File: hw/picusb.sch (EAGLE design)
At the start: 38 parts, among them Q1 BSS138, Q2 BSS138, Q3 BSS84, Q4 BSS84, U1 PIC16F1454SOIC, U2 AP7115W, X1 MINI-USB-UX60-MB-5ST

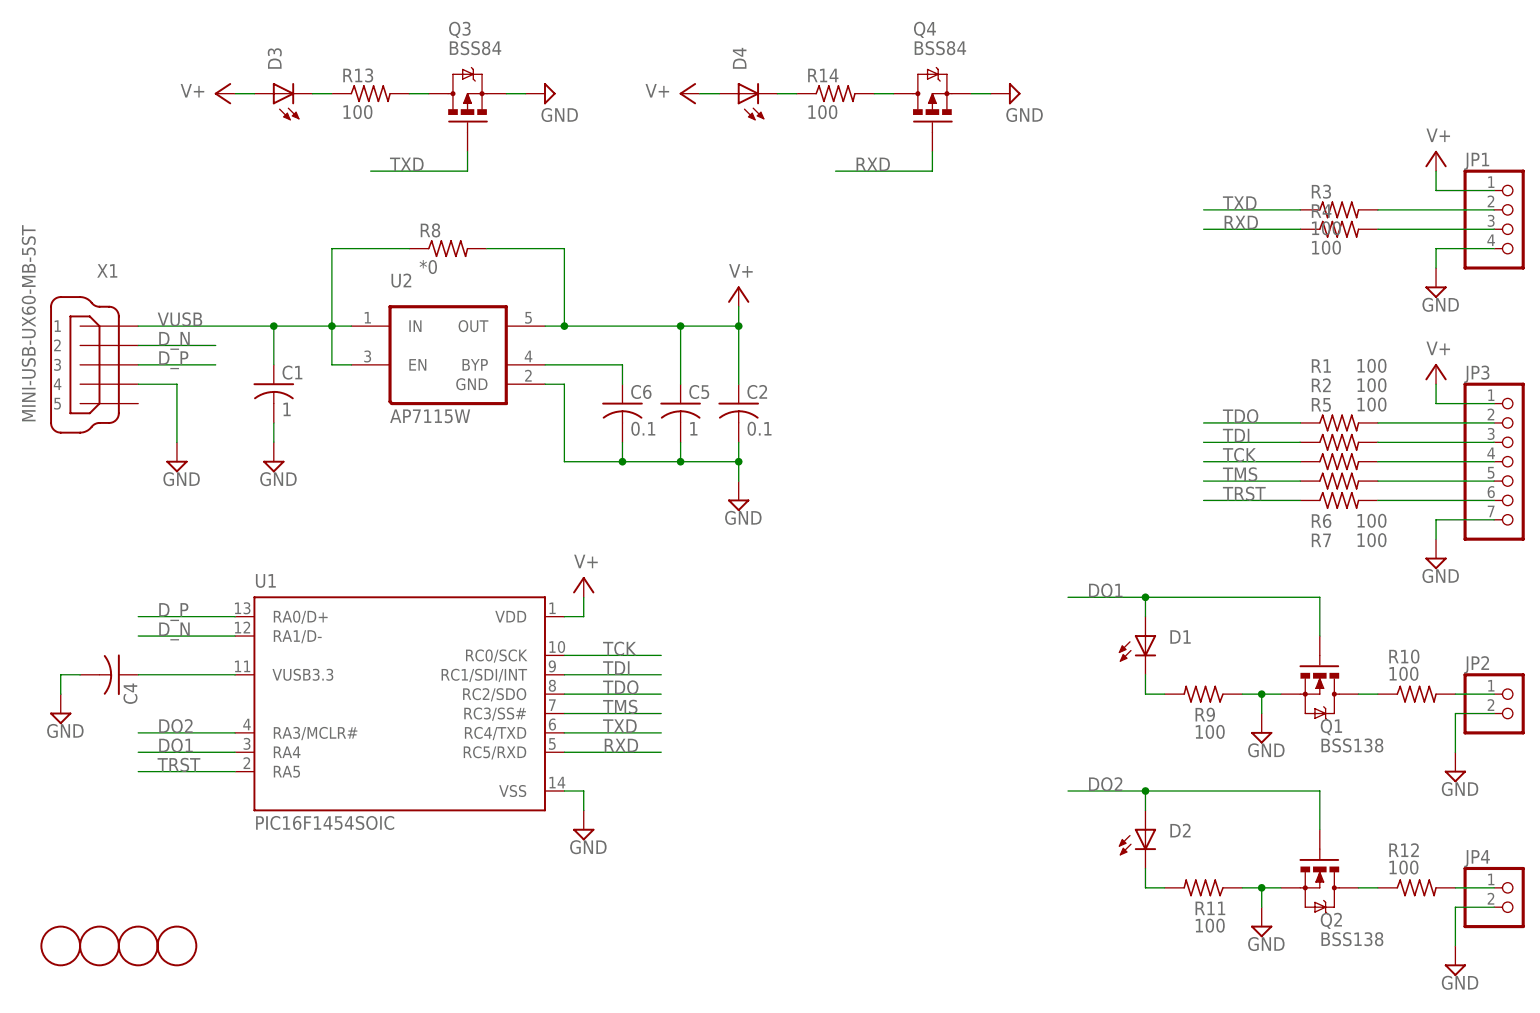
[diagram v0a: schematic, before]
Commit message: use 0805 LEDs
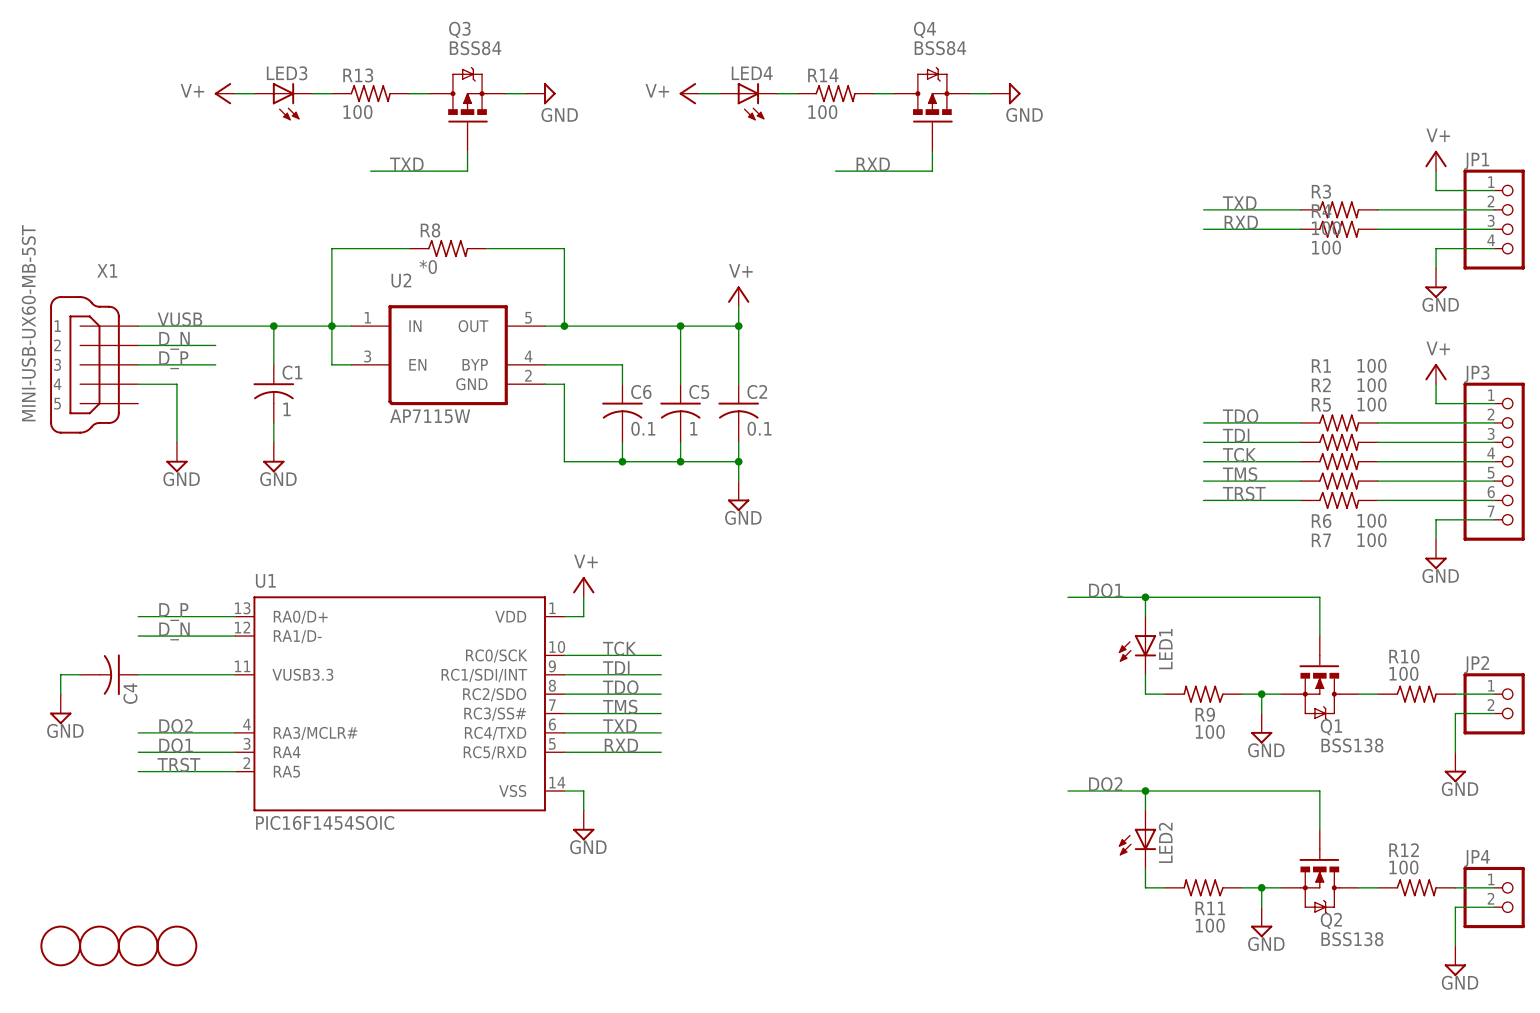
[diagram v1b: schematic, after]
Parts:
- removed D1, D2, D3, D4: (no value), SparkFun:LED0603
- added LED1, LED2, LED3, LED4: (no value), led:LEDCHIP-LED0805
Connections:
- net DO1: now also LED1.A; no longer D1.A
- net DO2: now also LED2.A; no longer D2.A
- net N$14: now also LED3.C; no longer D3.C
- net N$17: now also LED2.C; no longer D2.C
- net N$18: now also LED4.C; no longer D4.C
- net N$8: now also LED1.C; no longer D1.C
- net V+: now also LED3.A, LED4.A; no longer D3.A, D4.A
